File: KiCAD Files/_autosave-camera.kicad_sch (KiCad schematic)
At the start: 3 parts, among them J3 Micro_SD_Card_Det2, U1 K230_Rewired, U2 ZDSD04GLGEAG

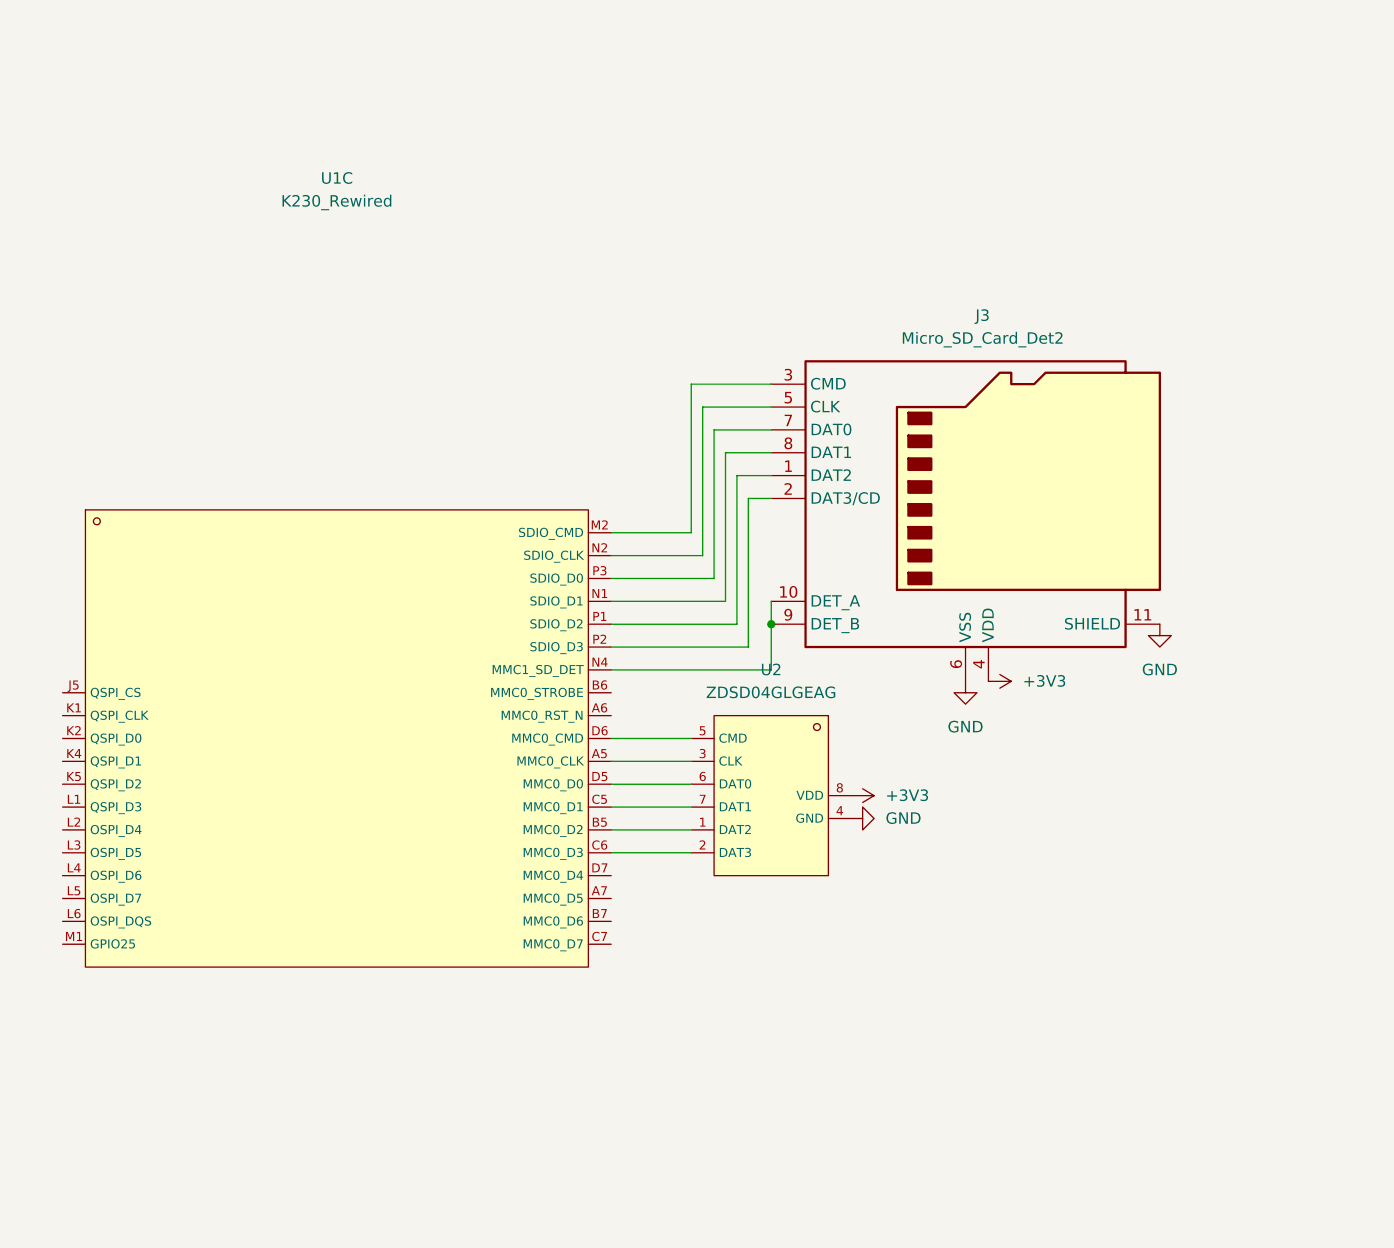
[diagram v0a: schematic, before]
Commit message: more peripherals
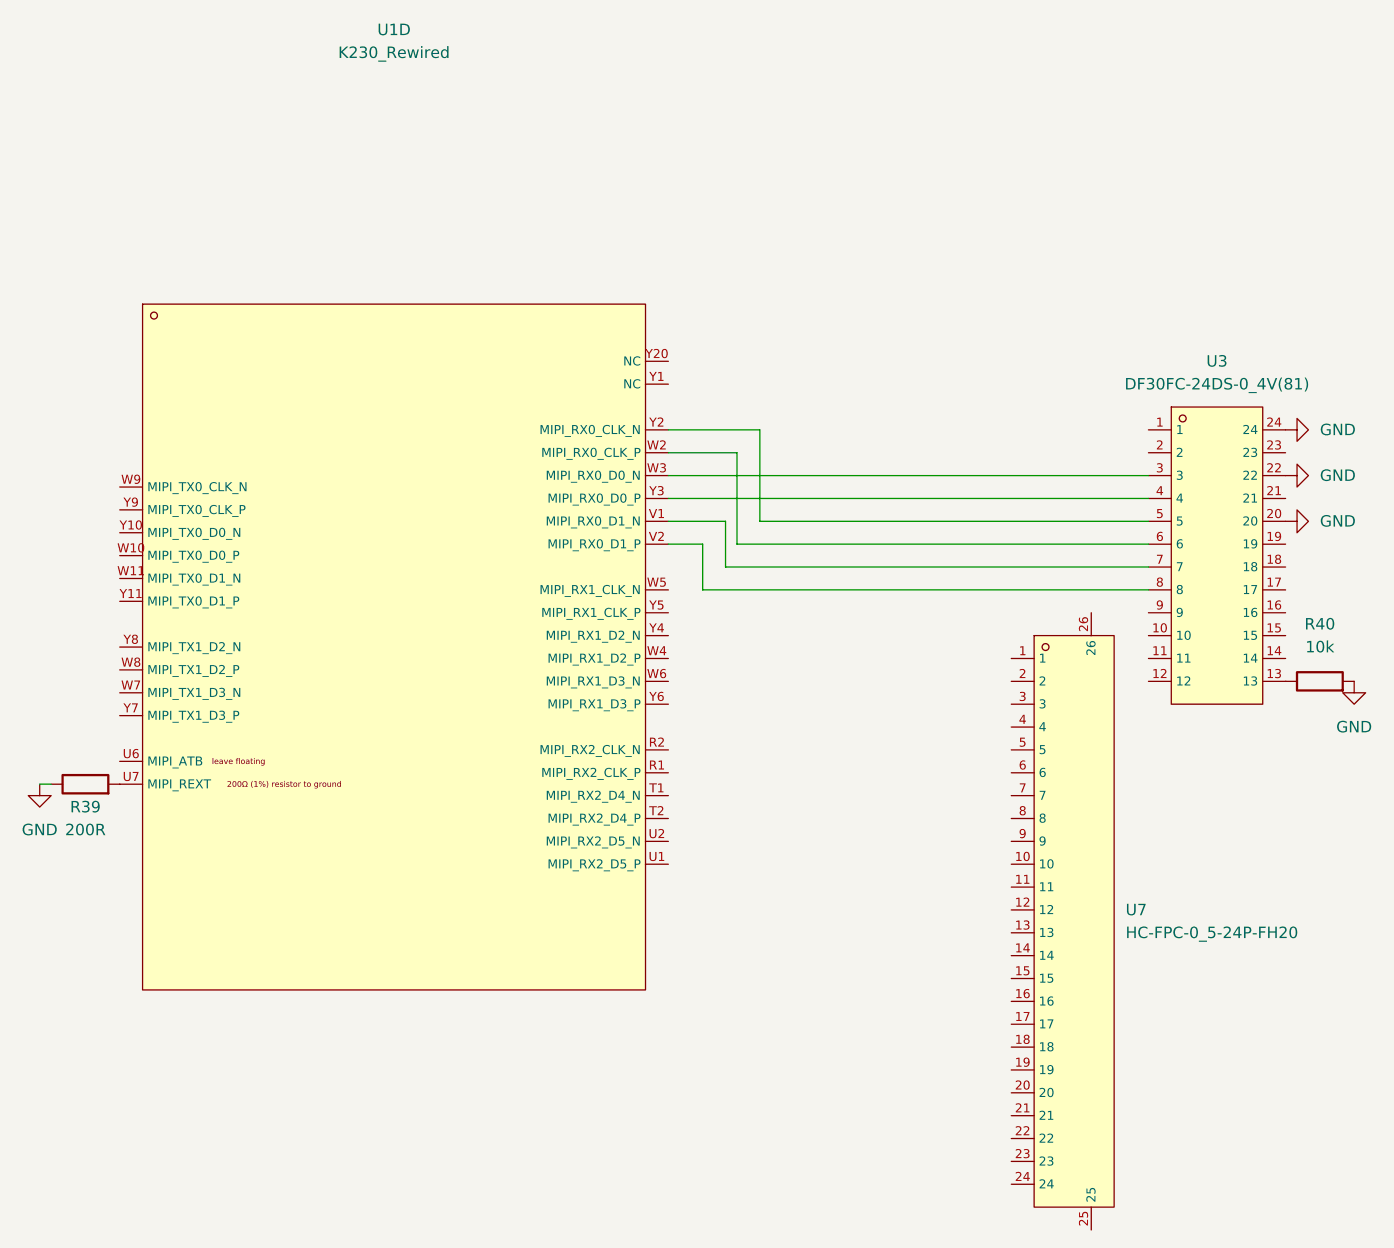
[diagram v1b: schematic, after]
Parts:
- removed J3: Micro_SD_Card_Det2, Connector_Card:microSD_HC_Molex_104031-0811, symbol Connector:Micro_SD_Card_Det2
- removed U1: K230_Rewired, footprints:BGA-390_L13.0-W13.0-P0.65-TL_C9900054646, symbol LCSC:K230_Rewired
- removed U2: ZDSD04GLGEAG, footprints:LGA-8_L8.0-W6.0-P1.27-TL-1, symbol LCSC:ZDSD04GLGEAG
- added R39: 200R, Resistor_SMD:R_0201_0603Metric, symbol Device:R
- added R40: 10k, Resistor_SMD:R_0402_1005Metric, symbol Device:R
- added U1: K230_Rewired, footprints:BGA-390_L13.0-W13.0-P0.65-TL_C9900054646, symbol LCSC:K230_Rewired
- added U3: DF30FC-24DS-0_4V(81), footprints:CONN-SMD_DF30FC-24DS-0.4V-82, symbol LCSC:DF30FC-24DS-0_4V(81)
- added U7: HC-FPC-0_5-24P-FH20, footprints:FPC-SMD_24P-P0.50_HC-FPC-0.5-24P-FH20, symbol LCSC:HC-FPC-0_5-24P-FH20
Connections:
- net GND: now also R39.1, R40.2, U3.20, U3.22, U3.24
- new net: R39.2, U1.U7 (MIPI_REXT)
- new net: R40.1, U3.13
- new net: U1.W3 (MIPI_RX0_D0_N), U3.3
- new net: U1.Y3 (MIPI_RX0_D0_P), U3.4
- new net: U1.Y2 (MIPI_RX0_CLK_N), U3.5
- new net: U1.W2 (MIPI_RX0_CLK_P), U3.6
- new net: U1.V1 (MIPI_RX0_D1_N), U3.7
- new net: U1.V2 (MIPI_RX0_D1_P), U3.8
